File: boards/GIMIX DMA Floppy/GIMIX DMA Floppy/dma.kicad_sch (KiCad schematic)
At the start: 10 parts, among them U30 74LS161, U31 74LS161, U32 74LS161, U33 74LS161, U38 74LS367, U45 74LS244, U46 74LS244, U54 74LS161

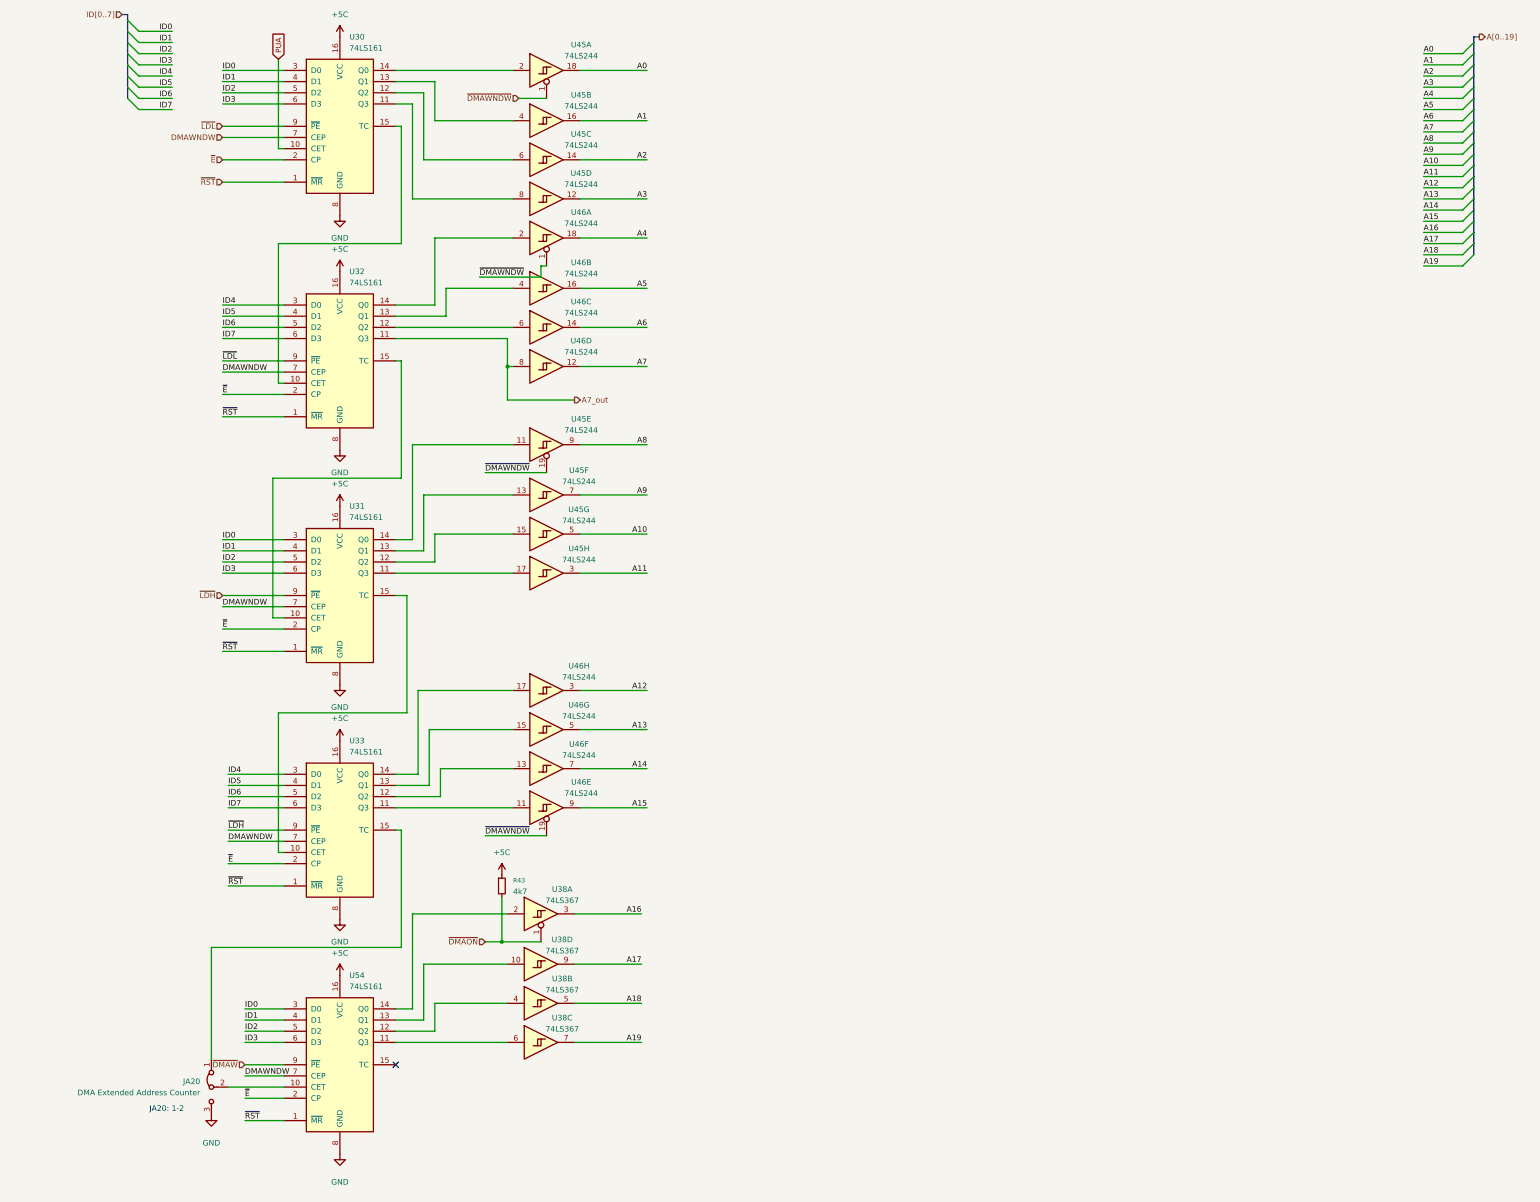
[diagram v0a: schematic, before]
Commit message: DMA Floppy update, silkscreen and gerbers added
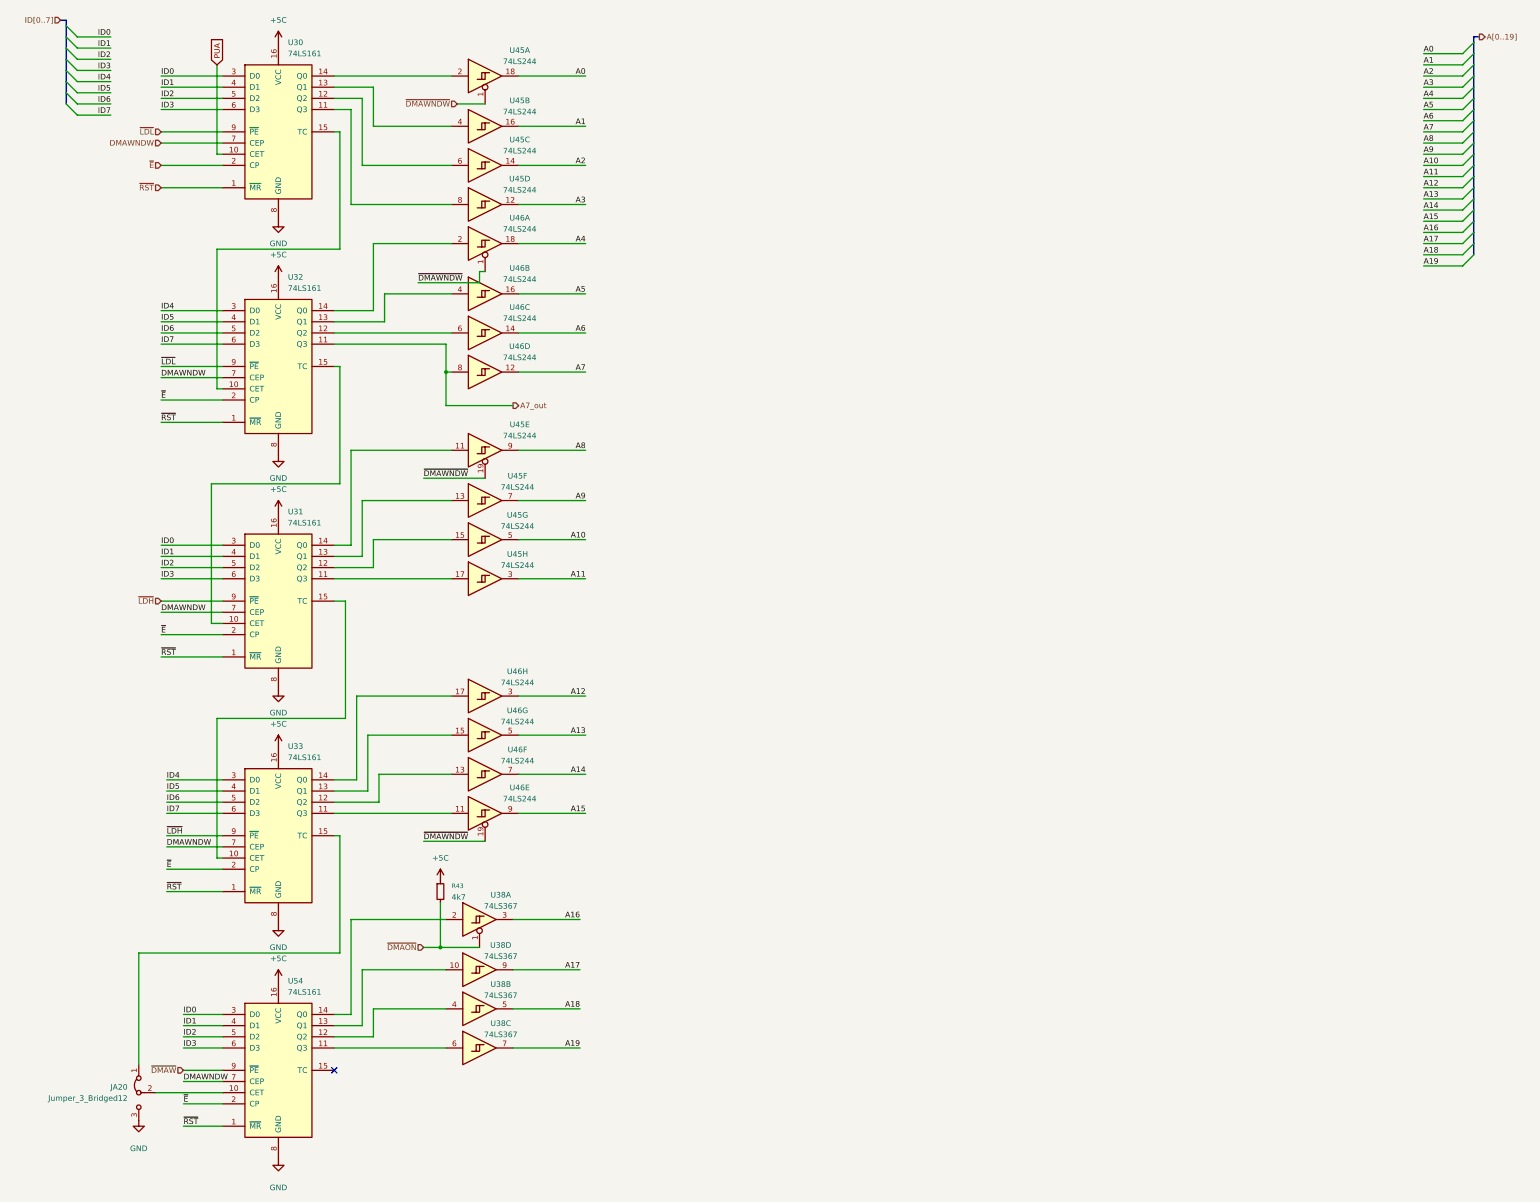
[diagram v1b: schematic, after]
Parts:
- JA20: value DMA Extended Address Counter -> Jumper_3_Bridged12
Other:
- note removed: "JA20: 1-2"
- moved on the sheet: JA20, R43, U30, U31, U32, U33, U38A, U38B, U38C, U38D, U45A, U45B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
